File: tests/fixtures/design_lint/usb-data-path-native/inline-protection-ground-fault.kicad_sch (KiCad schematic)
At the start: 3 parts, among them J1 USB_A, U1 UsbPhy, U2 UsbProtection

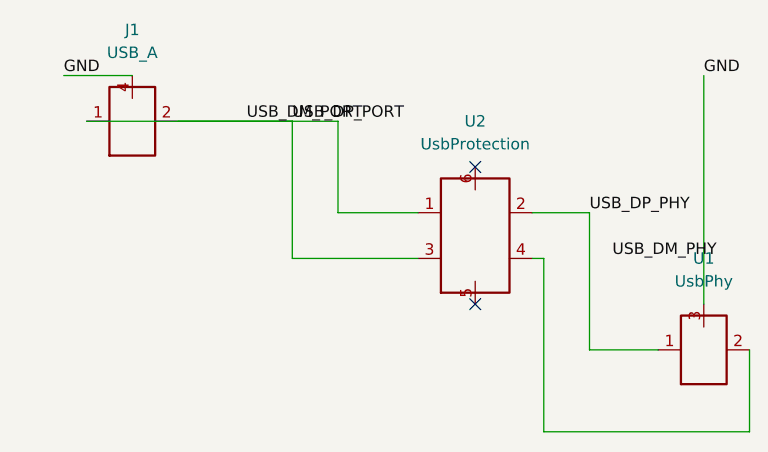
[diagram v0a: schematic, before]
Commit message: test: reroute synthetic inline USB fixtures
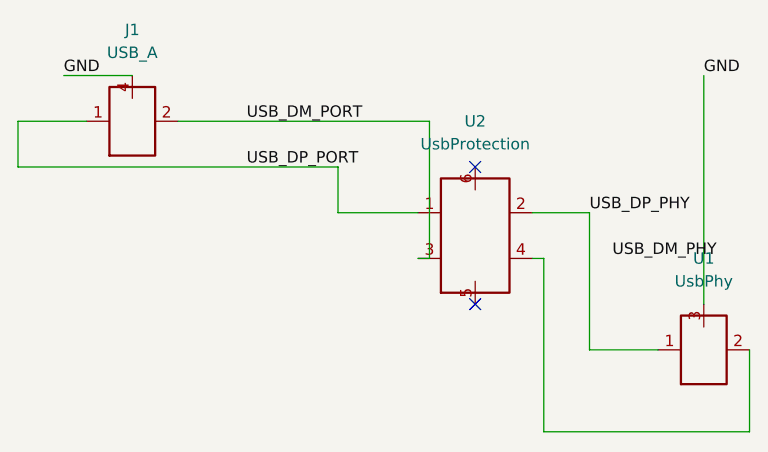
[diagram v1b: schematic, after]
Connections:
- net USB_DM_PORT: no longer J1.1 (D+), U2.1 (PORT_DP)
- new net USB_DP_PORT: J1.1 (D+), U2.1 (PORT_DP)
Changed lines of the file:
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@@
     (pin "3")
     (instances (project "synthetic-usb-inline-ground-fault" (path "/51000000-0000-4000-8000-000000000401" (reference "U1") (unit 1)))))
-  (wire (pts (xy 58.42 63.50) (xy 86.36 63.50))
+  (wire (pts (xy 58.42 63.50) (xy 50.80 63.50))
     (stroke (width 0) (type default)))
-  (wire (pts (xy 86.36 63.50) (xy 86.36 73.66))
+  (wire (pts (xy 50.80 63.50) (xy 50.80 68.58))
+    (stroke (width 0) (type default)))
+  (wire (pts (xy 50.80 68.58) (xy 86.36 68.58))
+    (stroke (width 0) (type default)))
+  (wire (pts (xy 86.36 68.58) (xy 86.36 73.66))
     (stroke (width 0) (type default)))
   (wire (pts (xy 86.36 73.66) (xy 95.25 73.66))
     (stroke (width 0) (type default)))
-  (label "USB_DP_PORT" (at 81.28 63.50 0)
+  (label "USB_DP_PORT" (at 76.20 68.58 0)
     (effects (font (size 1.27 1.27)) (justify left bottom))
 )
@@
     (effects (font (size 1.27 1.27)) (justify left bottom))
 )
-  (wire (pts (xy 68.58 63.50) (xy 81.28 63.50))
+  (wire (pts (xy 68.58 63.50) (xy 96.52 63.50))
     (stroke (width 0) (type default)))
-  (wire (pts (xy 81.28 63.50) (xy 81.28 78.74))
+  (wire (pts (xy 96.52 63.50) (xy 96.52 78.74))
     (stroke (width 0) (type default)))
-  (wire (pts (xy 81.28 78.74) (xy 95.25 78.74))
+  (wire (pts (xy 96.52 78.74) (xy 95.25 78.74))
     (stroke (width 0) (type default)))
   (label "USB_DM_PORT" (at 76.20 63.50 0)

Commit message: test: attach synthetic USB PHY label to route
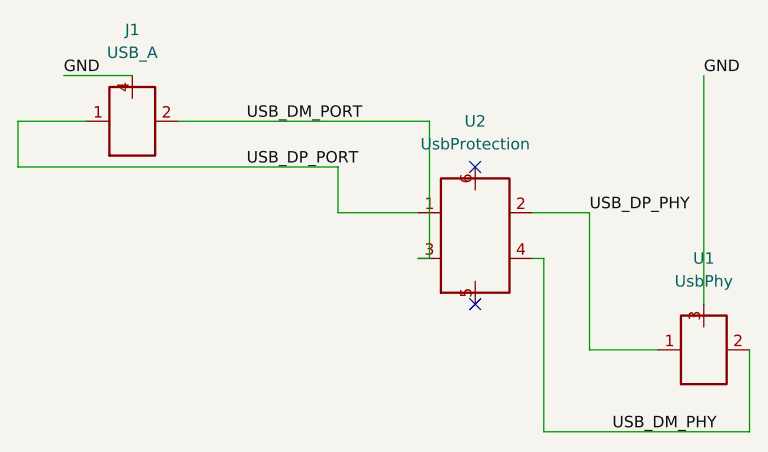
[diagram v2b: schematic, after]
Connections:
- net USB_DM_PHY: now also U1.2 (DM1), U2.4 (PHY_DM)
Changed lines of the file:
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@@
   (wire (pts (xy 132.08 98.00) (xy 132.08 88.90))
     (stroke (width 0) (type default)))
-  (label "USB_DM_PHY" (at 116.84 78.74 0)
+  (label "USB_DM_PHY" (at 116.84 98.00 0)
     (effects (font (size 1.27 1.27)) (justify left bottom))
 )
